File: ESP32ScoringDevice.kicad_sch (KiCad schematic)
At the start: 26 parts, among them J1 Conn_01x07, J2 Conn_01x03, J3 Conn_01x05, J4 Conn_01x04, J5 Conn_01x02, J6 Conn_01x02, J7 Conn_01x02, J8 Conn_01x02, Q1 BC337, Q2 BC337, U1 ESP32_DevKit_V1_DOIT

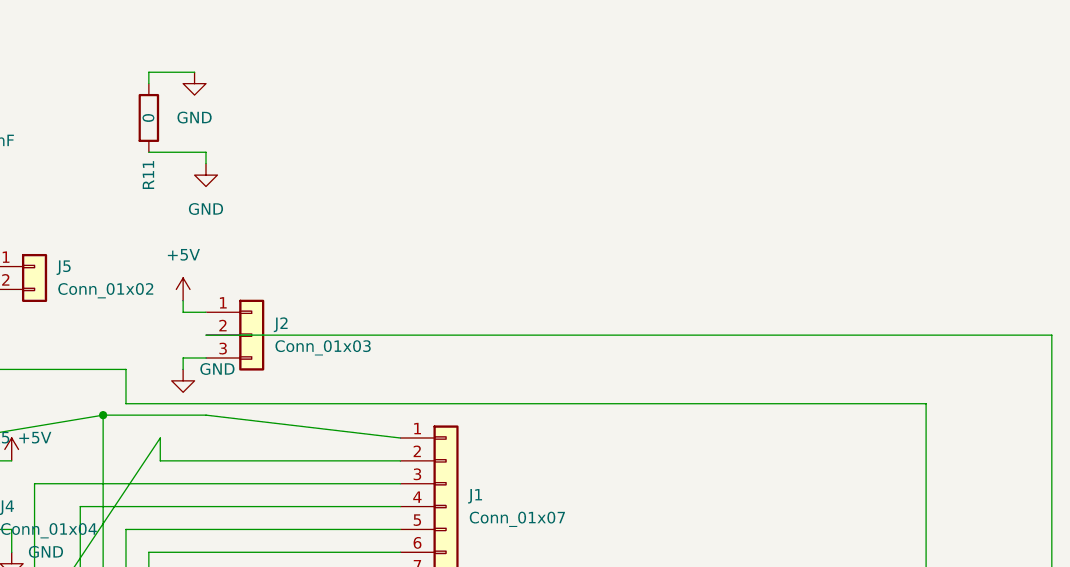
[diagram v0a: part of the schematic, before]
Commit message: Added 10k pull down resistor on the data line of the SW2812b matrices
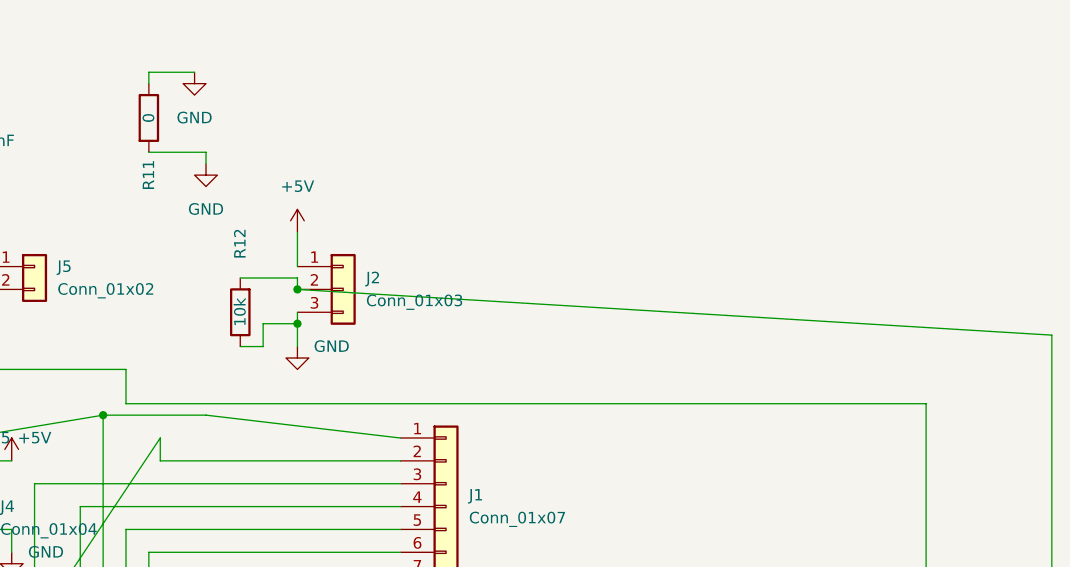
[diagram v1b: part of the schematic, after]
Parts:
- added R12: 10k, Resistor_THT:R_Axial_DIN0207_L6.3mm_D2.5mm_P10.16mm_Horizontal, symbol Device:R
- J4: footprint (none) -> Connector_PinHeader_2.54mm:PinHeader_1x04_P2.54mm_Vertical
- J5: footprint (none) -> Connector_PinHeader_2.54mm:PinHeader_1x02_P2.54mm_Vertical
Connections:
- net GND: now also R12.1
- net at J2.2 (Pin_2), U1.9 (IO26): now also R12.2
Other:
- moved on the sheet: J2
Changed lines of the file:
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@@
   (junction (at 68.58 30.48) (diameter 0) (color 0 0 0 0)
   )
+  (junction (at 114.3 48.26) (diameter 0) (color 0 0 0 0)
+  )
   (junction (at 135.89 97.79) (diameter 0) (color 0 0 0 0)
   )
@@
   (junction (at 67.31 22.86) (diameter 0) (color 0 0 0 0)
   )
+  (junction (at 114.3 44.45) (diameter 0) (color 0 0 0 0)
+  )
   (junction (at 50.8 114.3) (diameter 0) (color 0 0 0 0)
   )
@@
     (stroke (width 0) (type default) (color 0 0 0 0))
   )
+  (wire (pts (xy 114.3 48.26) (xy 114.3 50.8))
+    (stroke (width 0) (type default) (color 0 0 0 0))
+  )
   (wire (pts (xy 97.79 73.66) (xy 125.73 73.66))
     (stroke (width 0) (type default) (color 0 0 0 0))
@@
     (stroke (width 0) (type default) (color 0 0 0 0))
   )
-  (wire (pts (xy 101.6 52.07) (xy 101.6 53.34))
-    (stroke (width 0) (type default) (color 0 0 0 0))
-  )
   (wire (pts (xy 95.25 57.15) (xy 184.15 57.15))
     (stroke (width 0) (type default) (color 0 0 0 0))
@@
     (stroke (width 0) (type default) (color 0 0 0 0))
   )
-  (wire (pts (xy 104.14 52.07) (xy 101.6 52.07))
+  (wire (pts (xy 107.95 50.8) (xy 110.49 50.8))
     (stroke (width 0) (type default) (color 0 0 0 0))
   )
@@
     (stroke (width 0) (type default) (color 0 0 0 0))
   )
+  (wire (pts (xy 114.3 38.1) (xy 114.3 41.91))
+    (stroke (width 0) (type default) (color 0 0 0 0))
+  )
   (wire (pts (xy 54.61 109.22) (xy 102.87 109.22))
     (stroke (width 0) (type default) (color 0 0 0 0))
@@
     (stroke (width 0) (type default) (color 0 0 0 0))
   )
-  (wire (pts (xy 104.14 49.53) (xy 198.12 49.53))
+  (wire (pts (xy 114.3 44.45) (xy 198.12 49.53))
     (stroke (width 0) (type default) (color 0 0 0 0))
   )
@@
     (stroke (width 0) (type default) (color 0 0 0 0))
   )
-  (wire (pts (xy 101.6 45.72) (xy 101.6 46.99))
-    (stroke (width 0) (type default) (color 0 0 0 0))
-  )
   (wire (pts (xy 86.36 104.14) (xy 86.36 81.28))
     (stroke (width 0) (type default) (color 0 0 0 0))
@@
     (stroke (width 0) (type default) (color 0 0 0 0))
   )
-  (wire (pts (xy 101.6 46.99) (xy 104.14 46.99))
-    (stroke (width 0) (type default) (color 0 0 0 0))
-  )
   (wire (pts (xy 78.74 101.6) (xy 97.79 86.36))
     (stroke (width 0) (type default) (color 0 0 0 0))
@@
     (stroke (width 0) (type default) (color 0 0 0 0))
   )
+  (wire (pts (xy 114.3 43.18) (xy 114.3 44.45))
+    (stroke (width 0) (type default) (color 0 0 0 0))
+  )
   (wire (pts (xy 100.33 100.33) (xy 100.33 99.06))
     (stroke (width 0) (type default) (color 0 0 0 0))
@@
     (stroke (width 0) (type default) (color 0 0 0 0))
   )
+  (wire (pts (xy 110.49 48.26) (xy 114.3 48.26))
+    (stroke (width 0) (type default) (color 0 0 0 0))
+  )
   (wire (pts (xy 67.31 22.86) (xy 73.66 22.86))
     (stroke (width 0) (type default) (color 0 0 0 0))
@@
     (stroke (width 0) (type default) (color 0 0 0 0))
   )
+  (wire (pts (xy 114.3 46.99) (xy 114.3 48.26))
+    (stroke (width 0) (type default) (color 0 0 0 0))
+  )
   (wire (pts (xy 67.31 86.36) (xy 43.18 86.36))
     (stroke (width 0) (type default) (color 0 0 0 0))
@@
   )
   (wire (pts (xy 69.85 50.8) (xy 69.85 44.45))
+    (stroke (width 0) (type default) (color 0 0 0 0))
+  )
+  (wire (pts (xy 107.95 43.18) (xy 114.3 43.18))
+    (stroke (width 0) (type default) (color 0 0 0 0))
+  )
+  (wire (pts (xy 110.49 50.8) (xy 110.49 48.26))
     (stroke (width 0) (type default) (color 0 0 0 0))
   )
@@
       (effects (font (size 1.27 1.27)) (justify left))
     )
-    (property "Footprint" "" (id 2) (at 85.09 41.91 0)
+    (property "Footprint" "Connector_PinHeader_2.54mm:PinHeader_1x02_P2.54mm_Vertical" (id 2) (at 85.09 41.91 0)
       (effects (font (size 1.27 1.27)) hide)
     )
@@
     (pin "5")
   )
-  (symbol (lib_id "power:+5V") (at 101.6 45.72 0) (unit 1)
-    (in_bom yes) (on_board yes) (fields_autoplaced)
-    (property "Reference" "#PWR0107" (id 0) (at 101.6 49.53 0)
-      (effects (font (size 1.27 1.27)) hide)
-    )
-    (property "Value" "+5V" (id 1) (at 101.6 40.64 0))
-    (property "Footprint" "" (id 2) (at 101.6 45.72 0)
-      (effects (font (size 1.27 1.27)) hide)
-    )
-    (property "Datasheet" "" (id 3) (at 101.6 45.72 0)
-      (effects (font (size 1.27 1.27)) hide)
-    )
-    (pin "1")
+  (symbol (lib_id "power:+5V") (at 114.3 38.1 0) (unit 1)
+    (in_bom yes) (on_board yes) (fields_autoplaced)
+    (property "Reference" "#PWR0107" (id 0) (at 114.3 41.91 0)
+      (effects (font (size 1.27 1.27)) hide)
+    )
+    (property "Value" "+5V" (id 1) (at 114.3 33.02 0))
+    (property "Footprint" "" (id 2) (at 114.3 38.1 0)
+      (effects (font (size 1.27 1.27)) hide)
+    )
+    (property "Datasheet" "" (id 3) (at 114.3 38.1 0)
+      (effects (font (size 1.27 1.27)) hide)
+    )
+    (pin "1")
+  )
+  (symbol (lib_id "Device:R") (at 107.95 46.99 180) (unit 1)
+    (in_bom yes) (on_board yes)
+    (property "Reference" "R12" (id 0) (at 107.95 39.37 90))
+    (property "Value" "10k" (id 1) (at 107.95 46.99 90))
+    (property "Footprint" "Resistor_THT:R_Axial_DIN0207_L6.3mm_D2.5mm_P10.16mm_Horizontal" (id 2) (at 109.728 46.99 90)
+      (effects (font (size 1.27 1.27)) hide)
+    )
+    (property "Datasheet" "~" (id 3) (at 107.95 46.99 0)
+      (effects (font (size 1.27 1.27)) hide)
+    )
+    (pin "1")
+    (pin "2")
   )
   (symbol (lib_id "Connector_Generic:Conn_01x02") (at 171.45 105.41 0) (unit 1)
@@
     (pin "3")
   )
-  (symbol (lib_id "power:GND") (at 101.6 53.34 0) (unit 1)
-    (in_bom yes) (on_board yes)
-    (property "Reference" "#PWR0106" (id 0) (at 101.6 59.69 0)
-      (effects (font (size 1.27 1.27)) hide)
-    )
-    (property "Value" "GND" (id 1) (at 105.41 53.34 0))
-    (property "Footprint" "" (id 2) (at 101.6 53.34 0)
-      (effects (font (size 1.27 1.27)) hide)
-    )
-    (property "Datasheet" "" (id 3) (at 101.6 53.34 0)
+  (symbol (lib_id "power:GND") (at 114.3 50.8 0) (unit 1)
+    (in_bom yes) (on_board yes)
+    (property "Reference" "#PWR0106" (id 0) (at 114.3 57.15 0)
+      (effects (font (size 1.27 1.27)) hide)
+    )
+    (property "Value" "GND" (id 1) (at 118.11 50.8 0))
+    (property "Footprint" "" (id 2) (at 114.3 50.8 0)
+      (effects (font (size 1.27 1.27)) hide)
+    )
+    (property "Datasheet" "" (id 3) (at 114.3 50.8 0)
       (effects (font (size 1.27 1.27)) hide)
     )
@@
     (pin "1")
   )
-  (symbol (lib_id "Connector_Generic:Conn_01x03") (at 109.22 49.53 0) (unit 1)
-    (in_bom yes) (on_board yes) (fields_autoplaced)
-    (property "Reference" "J2" (id 0) (at 111.76 48.2599 0)
-      (effects (font (size 1.27 1.27)) (justify left))
-    )
-    (property "Value" "Conn_01x03" (id 1) (at 111.76 50.7999 0)
-      (effects (font (size 1.27 1.27)) (justify left))
-    )
-    (property "Footprint" "Connector_PinHeader_2.54mm:PinHeader_1x03_P2.54mm_Vertical" (id 2) (at 109.22 49.53 0)
-      (effects (font (size 1.27 1.27)) hide)
-    )
-    (property "Datasheet" "~" (id 3) (at 109.22 49.53 0)
+  (symbol (lib_id "Connector_Generic:Conn_01x03") (at 119.38 44.45 0) (unit 1)
+    (in_bom yes) (on_board yes) (fields_autoplaced)
+    (property "Reference" "J2" (id 0) (at 121.92 43.1799 0)
+      (effects (font (size 1.27 1.27)) (justify left))
+    )
+    (property "Value" "Conn_01x03" (id 1) (at 121.92 45.7199 0)
+      (effects (font (size 1.27 1.27)) (justify left))
+    )
+    (property "Footprint" "Connector_PinHeader_2.54mm:PinHeader_1x03_P2.54mm_Vertical" (id 2) (at 119.38 44.45 0)
+      (effects (font (size 1.27 1.27)) hide)
+    )
+    (property "Datasheet" "~" (id 3) (at 119.38 44.45 0)
       (effects (font (size 1.27 1.27)) hide)
     )
@@
       (effects (font (size 1.27 1.27)) (justify left))
     )
-    (property "Footprint" "" (id 2) (at 78.74 68.58 0)
+    (property "Footprint" "Connector_PinHeader_2.54mm:PinHeader_1x04_P2.54mm_Vertical" (id 2) (at 78.74 68.58 0)
       (effects (font (size 1.27 1.27)) hide)
     )
@@
       (reference "R11") (unit 1) (value "0") (footprint "Resistor_THT:R_Axial_DIN0207_L6.3mm_D2.5mm_P15.24mm_Horizontal")
     )
+    (path "/862a3167-2fce-48ad-a4a0-d810b4932066"
+      (reference "R12") (unit 1) (value "10k") (footprint "Resistor_THT:R_Axial_DIN0207_L6.3mm_D2.5mm_P10.16mm_Horizontal")
+    )
     (path "/6431a2d4-07b5-44af-af94-55c331dfc453"
